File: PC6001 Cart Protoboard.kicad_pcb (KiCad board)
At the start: 2 copper layers, 107.3 x 80.6 mm, 23 parts, among them J1 PC-6001 edge connector, SW1 PicoReset, SW2 EspReset, SW3 Button A, U2 ESP32-DevKitC, U3 74LS32, U4 microSD-Breakout, U5 74LS00, U6 SN74LVC245AN, U7 SN74LVC245AN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

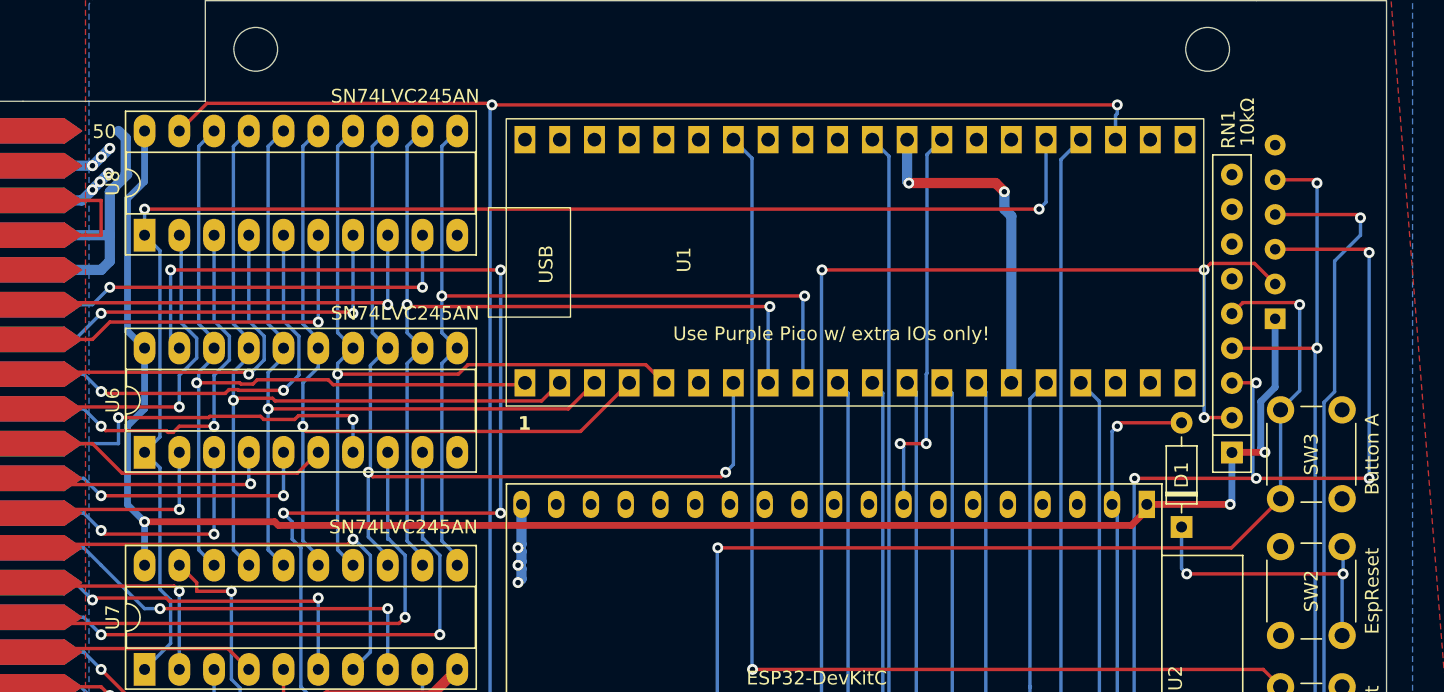
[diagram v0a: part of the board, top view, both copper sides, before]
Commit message: Source 3v3 from Pico for now
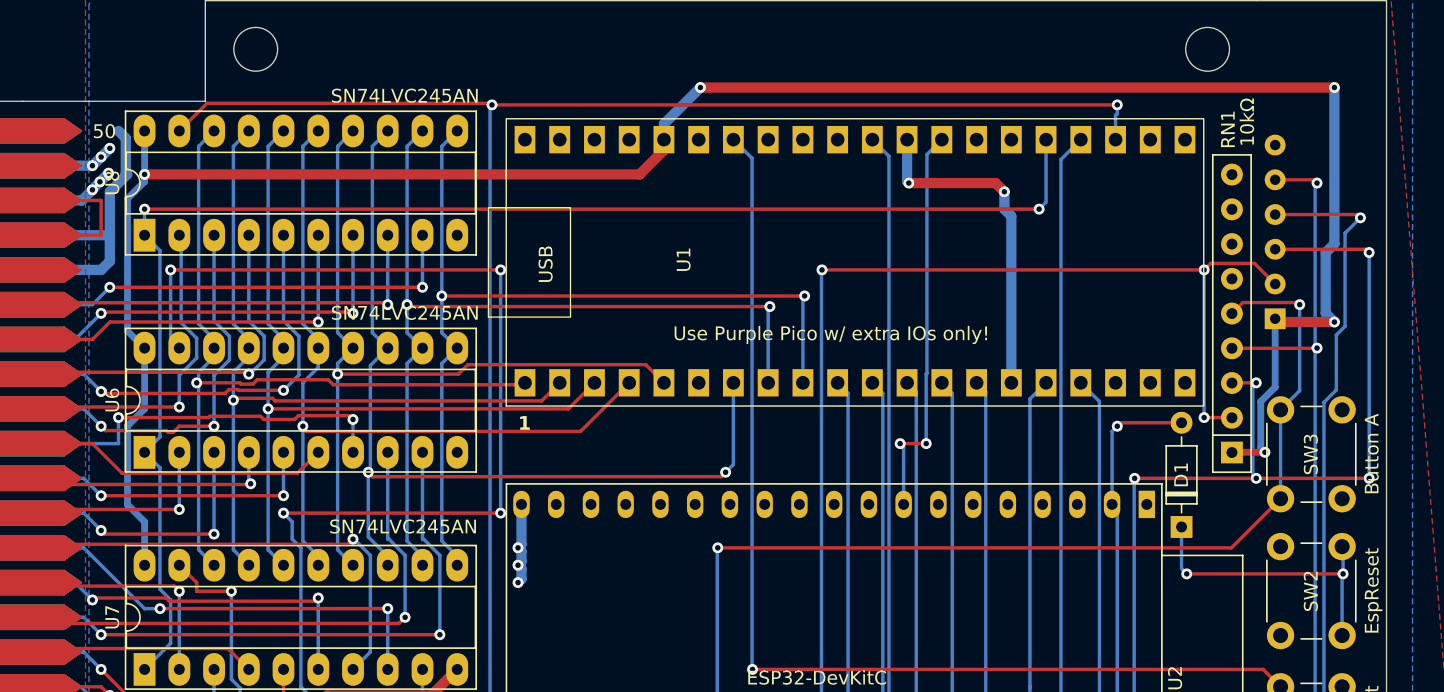
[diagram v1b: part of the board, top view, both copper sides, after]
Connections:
- U1 pad 36: unconnected-(U1-3v3-Pad36) -> +3.3V
- U2 pad 1: +3.3V -> unconnected-(U2-3V3-Pad1)
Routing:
- net +3.3V: track 130.8 -> 159.4 mm, vias 3 -> 5

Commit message: ESP_INT restored
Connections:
- U2 pad 11: /INT -> /ESP_INT
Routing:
- net /ESP_INT: track 0.00 -> 27.6 mm

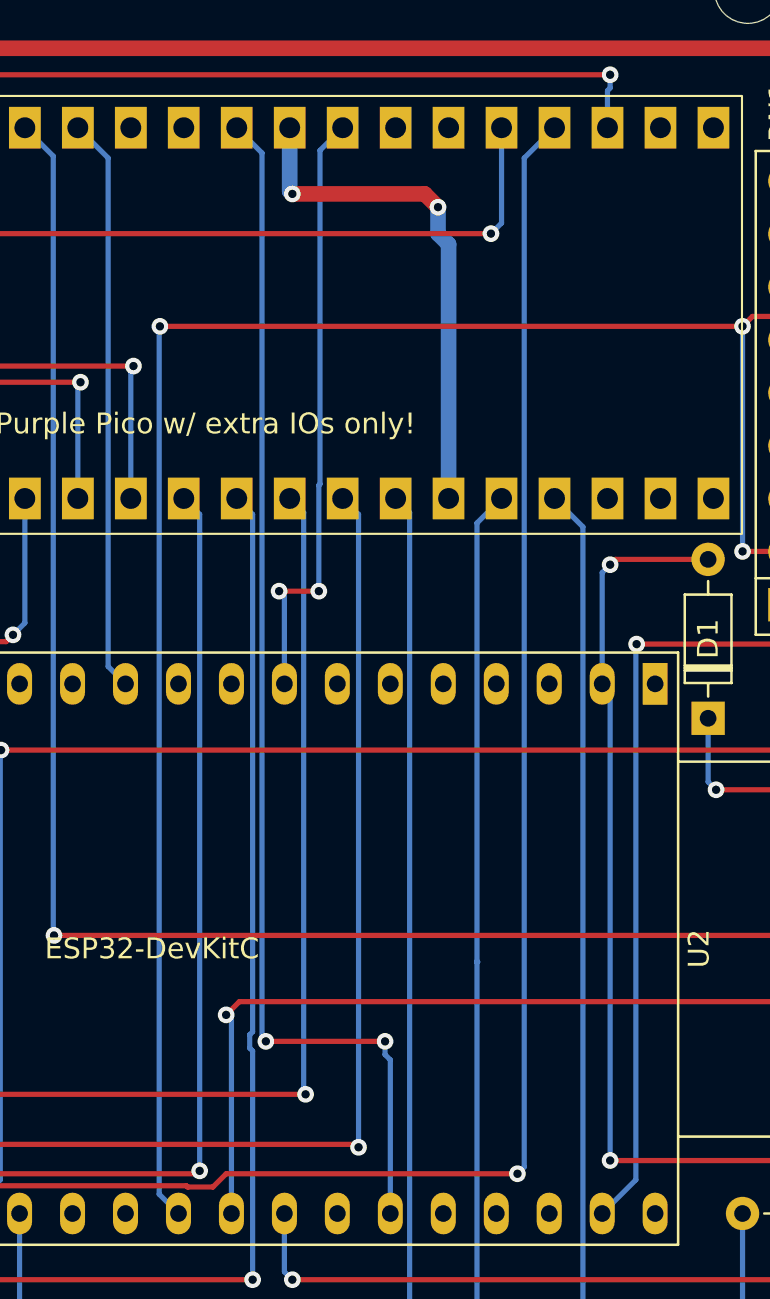
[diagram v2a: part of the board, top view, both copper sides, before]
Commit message: Restore ESP_CMD, ESP_PROC
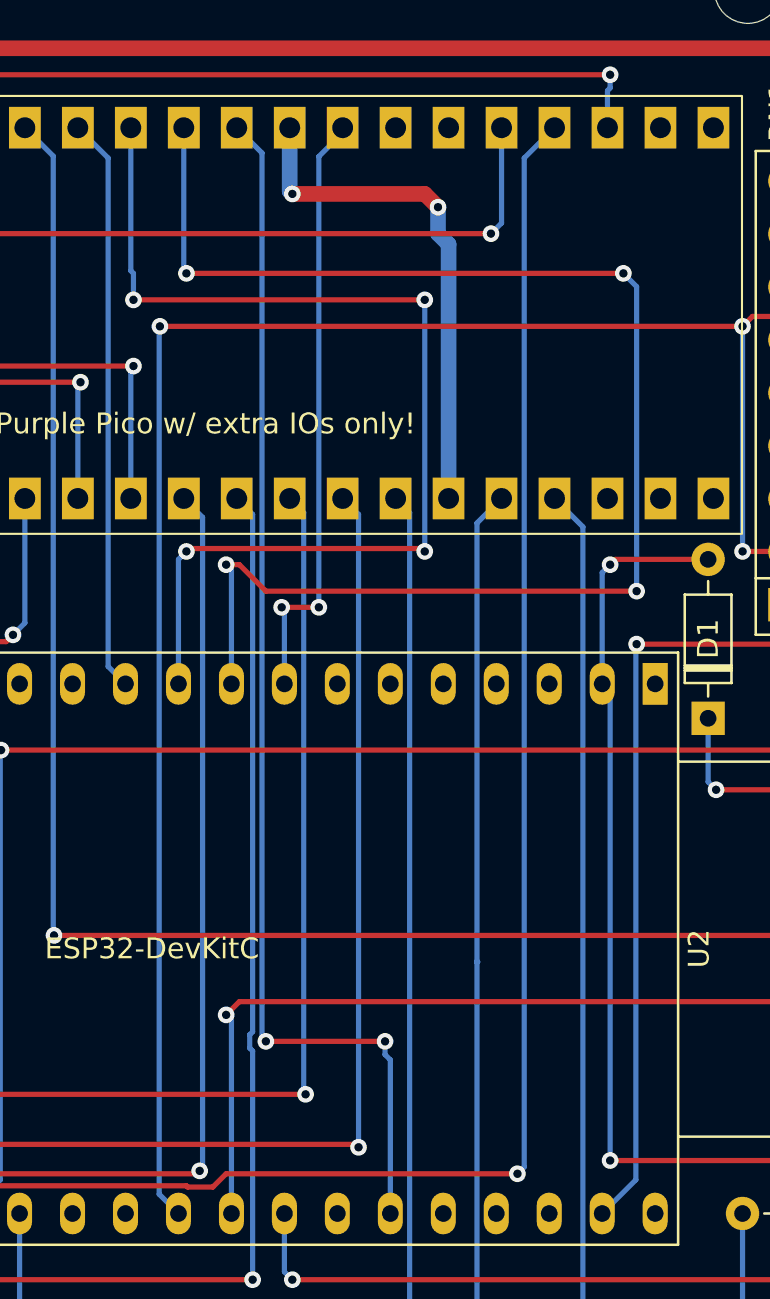
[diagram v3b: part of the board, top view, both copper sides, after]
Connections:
- U2 pad 10: /PROC -> /ESP_PROC
- U2 pad 9: /CMD -> /ESP_CMD
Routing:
- net /ESP_CMD: track 0.00 -> 69.5 mm, vias 0 -> 4
- net /ESP_PROC: track 0.00 -> 52.4 mm, vias 0 -> 4

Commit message: Frantically add caps
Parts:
- added C1: 0.1µF, Capacitor_THT:C_Disc_D5.0mm_W2.5mm_P2.50mm, F.Cu at (169.5, 137.2)
- added C2: 0.1µF, Capacitor_THT:C_Disc_D5.0mm_W2.5mm_P2.50mm, F.Cu at (174.0, 101.0)
- added C3: 0.1µF, Capacitor_THT:C_Disc_D5.0mm_W2.5mm_P2.50mm, F.Cu at (162.6, 73.0)
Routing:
- net +3.3V: track 159.4 -> 241.1 mm, vias 5 -> 8

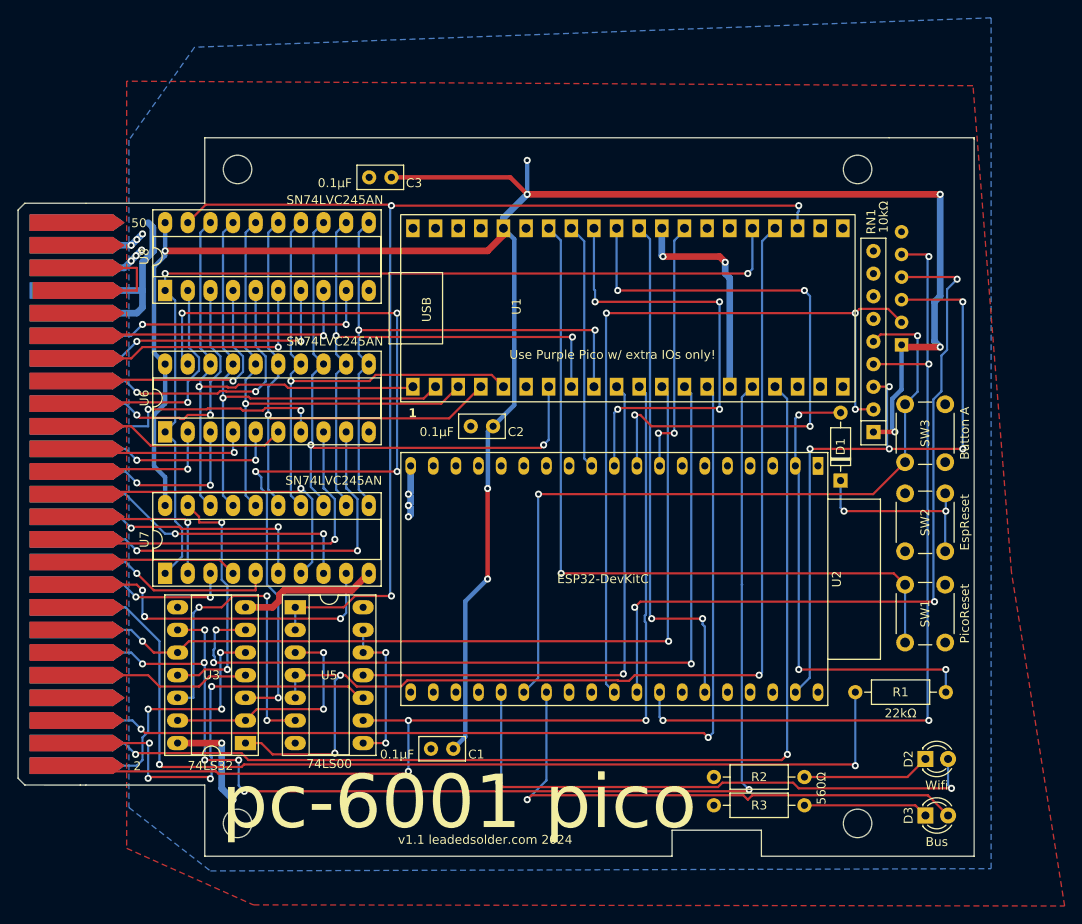
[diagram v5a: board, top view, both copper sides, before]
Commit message: Tie address buffer IN/out to always high
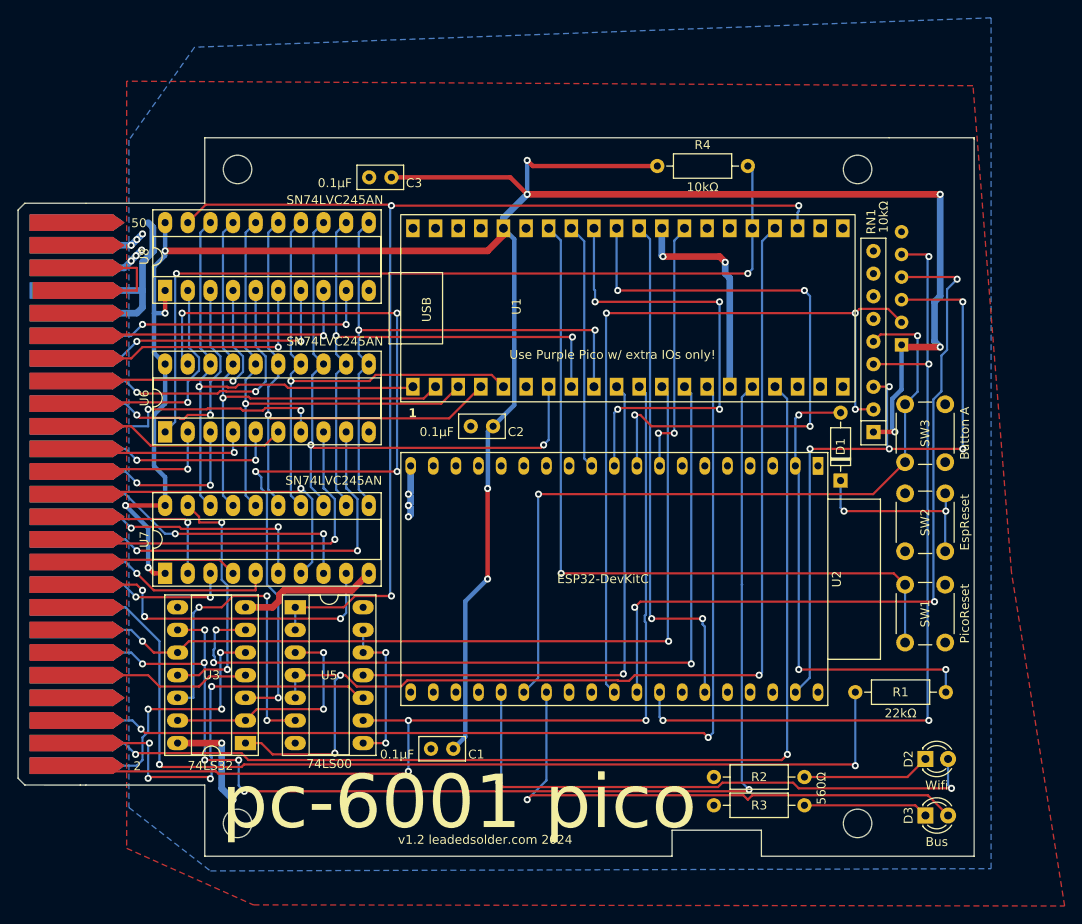
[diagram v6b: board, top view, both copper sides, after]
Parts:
- added R4: 10kΩ, Resistor_THT:R_Axial_DIN0207_L6.3mm_D2.5mm_P10.16mm_Horizontal, F.Cu at (192.4, 71.8)
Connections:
- U7 pad 1: /IN/~{OUT} -> +3.3V
- U8 pad 1: /IN/~{OUT} -> +3.3V
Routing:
- net +3.3V: track 241.1 -> 274.3 mm, vias 8 -> 11
- net /IN/~{OUT}: track 106.9 -> 94.9 mm
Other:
- board text added: "v1.2 leadedsolder.com 2024"
- board text removed: "v1.1 leadedsolder.com 2024"

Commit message: Safety pull-ups routed
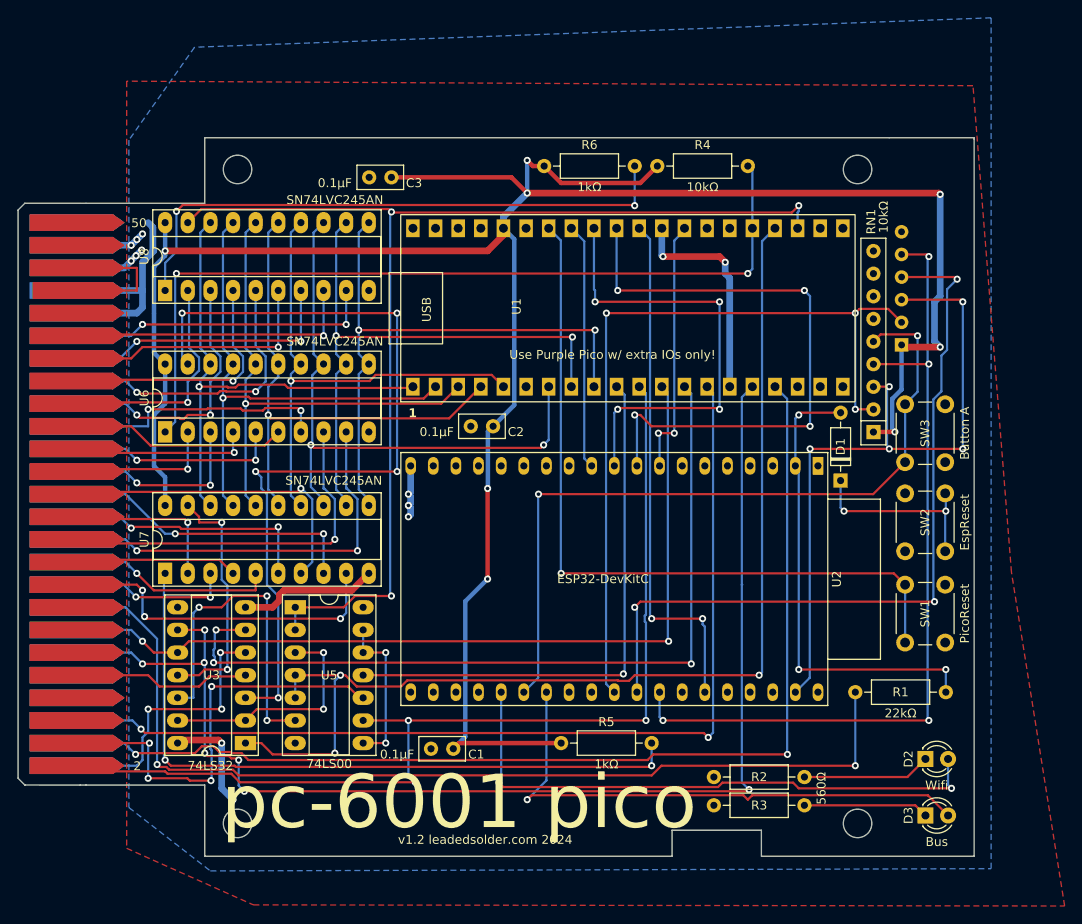
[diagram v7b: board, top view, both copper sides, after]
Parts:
- added R5: 1kΩ, Resistor_THT:R_Axial_DIN0207_L6.3mm_D2.5mm_P10.16mm_Horizontal, F.Cu at (181.6, 136.5)
- added R6: 1kΩ, Resistor_THT:R_Axial_DIN0207_L6.3mm_D2.5mm_P10.16mm_Horizontal, F.Cu at (179.7, 71.8)
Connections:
- U7 pad 1: +3.3V -> Net-(U7-DIR)
- U8 pad 1: +3.3V -> Net-(U8-DIR)
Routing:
- net Net-(U7-DIR): track 0.00 -> 78.6 mm, vias 0 -> 2
- net Net-(U8-DIR): track 0.00 -> 65.6 mm, vias 0 -> 2
- net +3.3V: track 274.3 -> 269.8 mm, vias 11 -> 8
- net /~{CS3}: track 116.5 -> 119.1 mm
- net /RESET: track 114.8 -> 115.6 mm
- net /~{DRD2}: track 126.2 -> 126.8 mm
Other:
- board text removed: "TODO: Place the '08 and '32 properly"
